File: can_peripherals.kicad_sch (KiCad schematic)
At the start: 5 parts

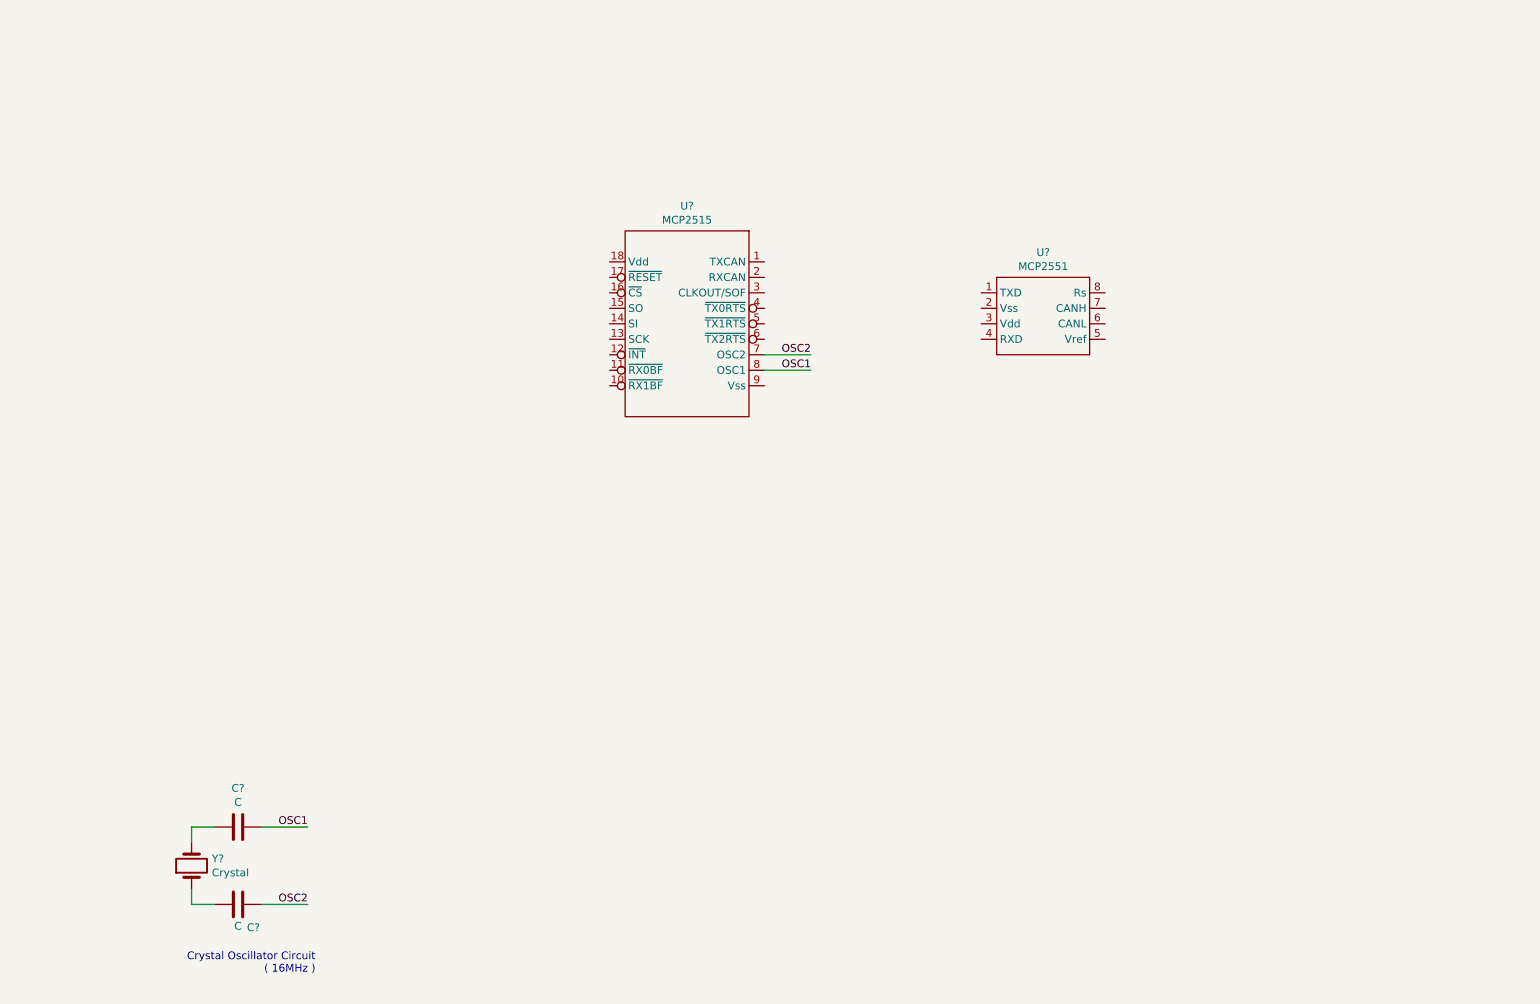
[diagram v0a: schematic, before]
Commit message: Added annotated reference numbers
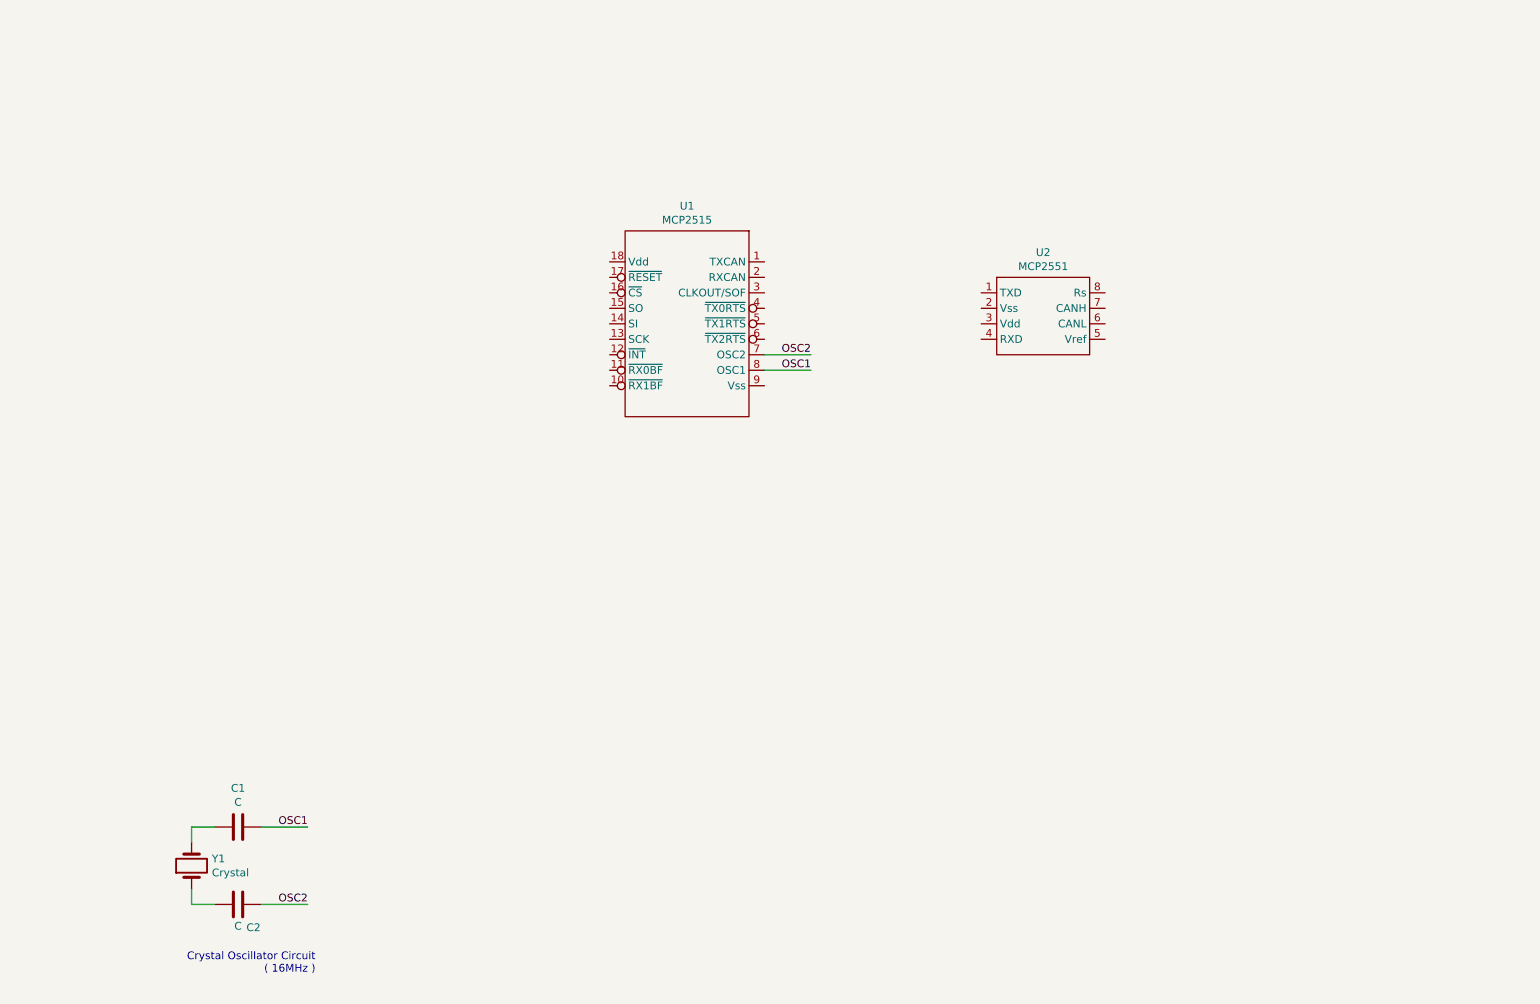
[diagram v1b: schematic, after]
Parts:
- gave numbers to parts that had none: 5
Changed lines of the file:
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@@
   (symbol (lib_id "Device:C") (at 59.69 157.48 90) (unit 1)
     (in_bom yes) (on_board yes)
-    (property "Reference" "C?" (id 0) (at 59.69 151.1108 90))
+    (property "Reference" "C1" (id 0) (at 59.69 151.1108 90))
     (property "Value" "C" (id 1) (at 59.69 153.4095 90))
     (property "Footprint" "" (id 2) (at 63.5 156.5148 0)
@@
   (symbol (lib_id "Device:C") (at 59.69 170.18 90) (unit 1)
     (in_bom yes) (on_board yes)
-    (property "Reference" "C?" (id 0) (at 62.23 173.9708 90))
+    (property "Reference" "C2" (id 0) (at 62.23 173.9708 90))
     (property "Value" "C" (id 1) (at 59.69 173.7295 90))
     (property "Footprint" "" (id 2) (at 63.5 169.2148 0)
@@
   (symbol (lib_id "Device:Crystal") (at 52.07 163.83 90) (unit 1)
     (in_bom yes) (on_board yes)
-    (property "Reference" "Y?" (id 0) (at 55.3975 162.6806 90)
+    (property "Reference" "Y1" (id 0) (at 55.3975 162.6806 90)
       (effects (font (size 1.27 1.27)) (justify right))
     )
@@
   (symbol (lib_id "symbols:MCP2551") (at 191.77 74.93 0) (unit 1)
     (in_bom yes) (on_board yes)
-    (property "Reference" "U?" (id 0) (at 191.77 63.2268 0))
+    (property "Reference" "U2" (id 0) (at 191.77 63.2268 0))
     (property "Value" "MCP2551" (id 1) (at 191.77 65.5255 0))
     (property "Footprint" "Package_SO:SO-8_3.9x4.9mm_P1.27mm" (id 2) (at 196.85 44.45 0)
@@
   (symbol (lib_id "symbols:MCP2515") (at 133.35 74.93 0) (mirror y) (unit 1)
     (in_bom yes) (on_board yes)
-    (property "Reference" "U?" (id 0) (at 133.35 55.6068 0))
+    (property "Reference" "U1" (id 0) (at 133.35 55.6068 0))
     (property "Value" "MCP2515" (id 1) (at 133.35 57.9055 0))
     (property "Footprint" "Package_SO:SOIC-18W_7.5x11.6mm_P1.27mm" (id 2) (at 128.27 44.45 0)

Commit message: Finished CAN peripheral
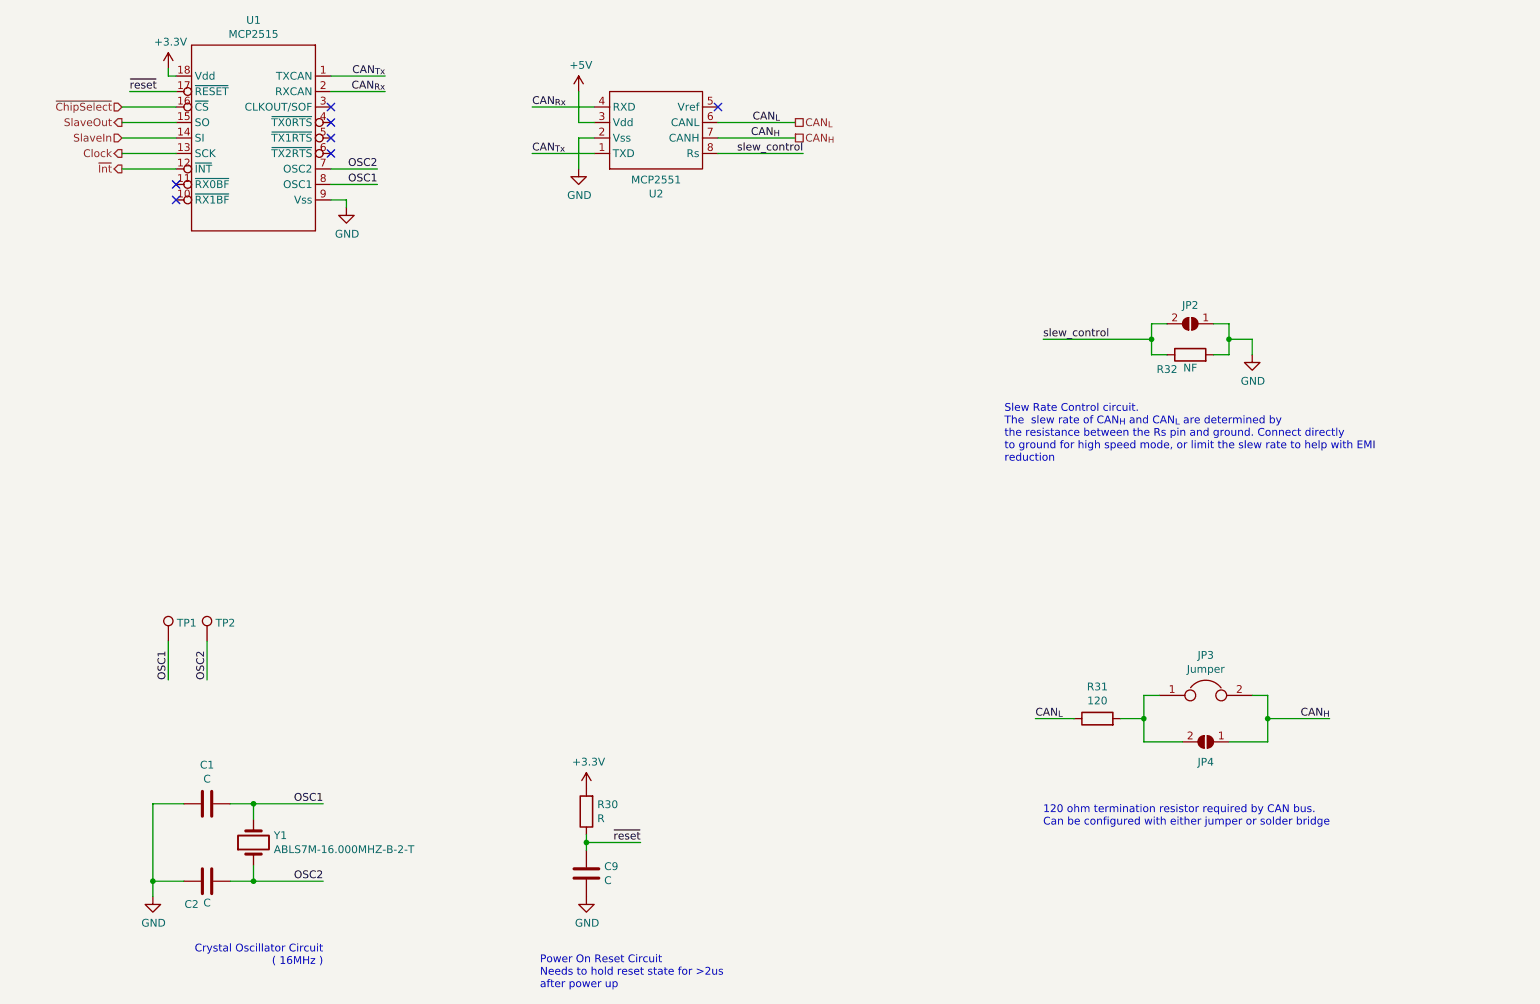
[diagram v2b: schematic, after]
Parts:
- removed Y1: Crystal, symbol Device:Crystal
- added C9: C, symbol Device:C
- added JP2, JP4: SolderJumper_2_Open, symbol Jumper:SolderJumper_2_Open
- added JP3: Jumper, symbol Device:Jumper
- added R30: R, symbol Device:R
- added R31: 120, symbol Device:R
- added R32: NF, symbol Device:R
- added TP1, TP2: TestPoint, symbol Connector:TestPoint
- added Y1: ABLS7M-16.000MHZ-B-2-T, symbol symbols:ABLS7M-16.000MHZ-B-2-T
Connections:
- net OSC1: now also C1.1, TP1.1, Y1.2; no longer C1.2
- net OSC2: now also C2.1, TP2.1, Y1.1; no longer C2.2
- net CAN_{Tx}: now reaches U2.1 (TXD)
- net CAN_{Tx}: now also U1.1 (TXCAN)
- net GND: now reaches U2.2 (Vss)
- net GND: now also C1.2, C2.2, U1.9 (Vss), C9.2, JP2.1 (A), R32.2
- net +5V: now reaches U2.3 (Vdd)
- net CAN_{Rx}: now reaches U2.4 (RXD)
- net CAN_{Rx}: now also U1.2 (RXCAN)
- net CAN_{L}: now reaches U2.6 (CANL)
- net CAN_{L}: now also R31.1
- net CAN_{H}: now reaches U2.7 (CANH)
- net CAN_{H}: now also JP3.2, JP4.1 (A)
- net slew_control: now reaches U2.8 (Rs)
- net slew_control: now also JP2.2 (B), R32.1
- net ~Int: now reaches U1.12 (~INT)
- net Clock: now reaches U1.13 (SCK)
- net SlaveIn: now reaches U1.14 (SI)
- net SlaveOut: now reaches U1.15 (SO)
- net ~ChipSelect: now reaches U1.16 (~CS)
- net ~reset: now reaches U1.17 (~RESET)
- net ~reset: now also C9.1, R30.1
- net +3V3: now reaches U1.18 (Vdd)
- net +3V3: now also R30.2
- new net: JP3.1, JP4.2 (B), R31.2
- no-connect marks 0 -> 7
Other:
- note added: "120 ohm termination resistor required by CAN bus. Can be configured with either jumper or solder bridge"
- note added: "Power On Reset Circuit Needs to hold reset state for >2us after power up"
- note added: "Slew Rate Control circuit. The slew rate of CAN_{H} and CAN_{L} are determined by the resistance between the Rs pin and ground. Connect directly to ground for high speed mode, or limit the slew rate to help with EMI reduction"
- moved on the sheet: C1, C2, U1, U2
